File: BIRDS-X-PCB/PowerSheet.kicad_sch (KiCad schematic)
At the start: 28 parts, among them J201 Conn_01x02, J202 Conn_01x02, J203 Conn_01x02, Q201 AO3420, Q202 AO3420, U201 LTC4361-2, U202 LTC4361-2, U203 0.1S7B_0512S3UP

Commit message: Fix all DRC
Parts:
- removed JP201, JP202: Jumper_2_Open, Jumper:SolderJumper-2_P1.3mm_Open_RoundedPad1.0x1.5mm, symbol Jumper:Jumper_2_Open
- added Q502 (x2): 2N7002, Package_TO_SOT_SMD:SOT-23, symbol Transistor_FET:2N7002
- added R206, R207: 1M, Resistor_SMD:R_0603_1608Metric_Pad0.98x0.95mm_HandSolder, symbol Device:R
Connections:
- net DIO1_3V3_EN_FROM_BOSS: now also Q502.1 (G); no longer U202.1 (~{ON})
- net DIO2_5V_EN_FROM_BOSS: now also Q502.1 (G); no longer U201.1 (~{ON})
- net GND: now also Q502.2 (S), Q502.2 (S)
- net SUP_3V3: now also R207.1
- net SUP_5V0: now also R206.1
- new net: Q502.3 (D), R206.2, U201.1 (~{ON})
- new net: Q502.3 (D), R207.2, U202.1 (~{ON})
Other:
- note added: "Basic Inverter"

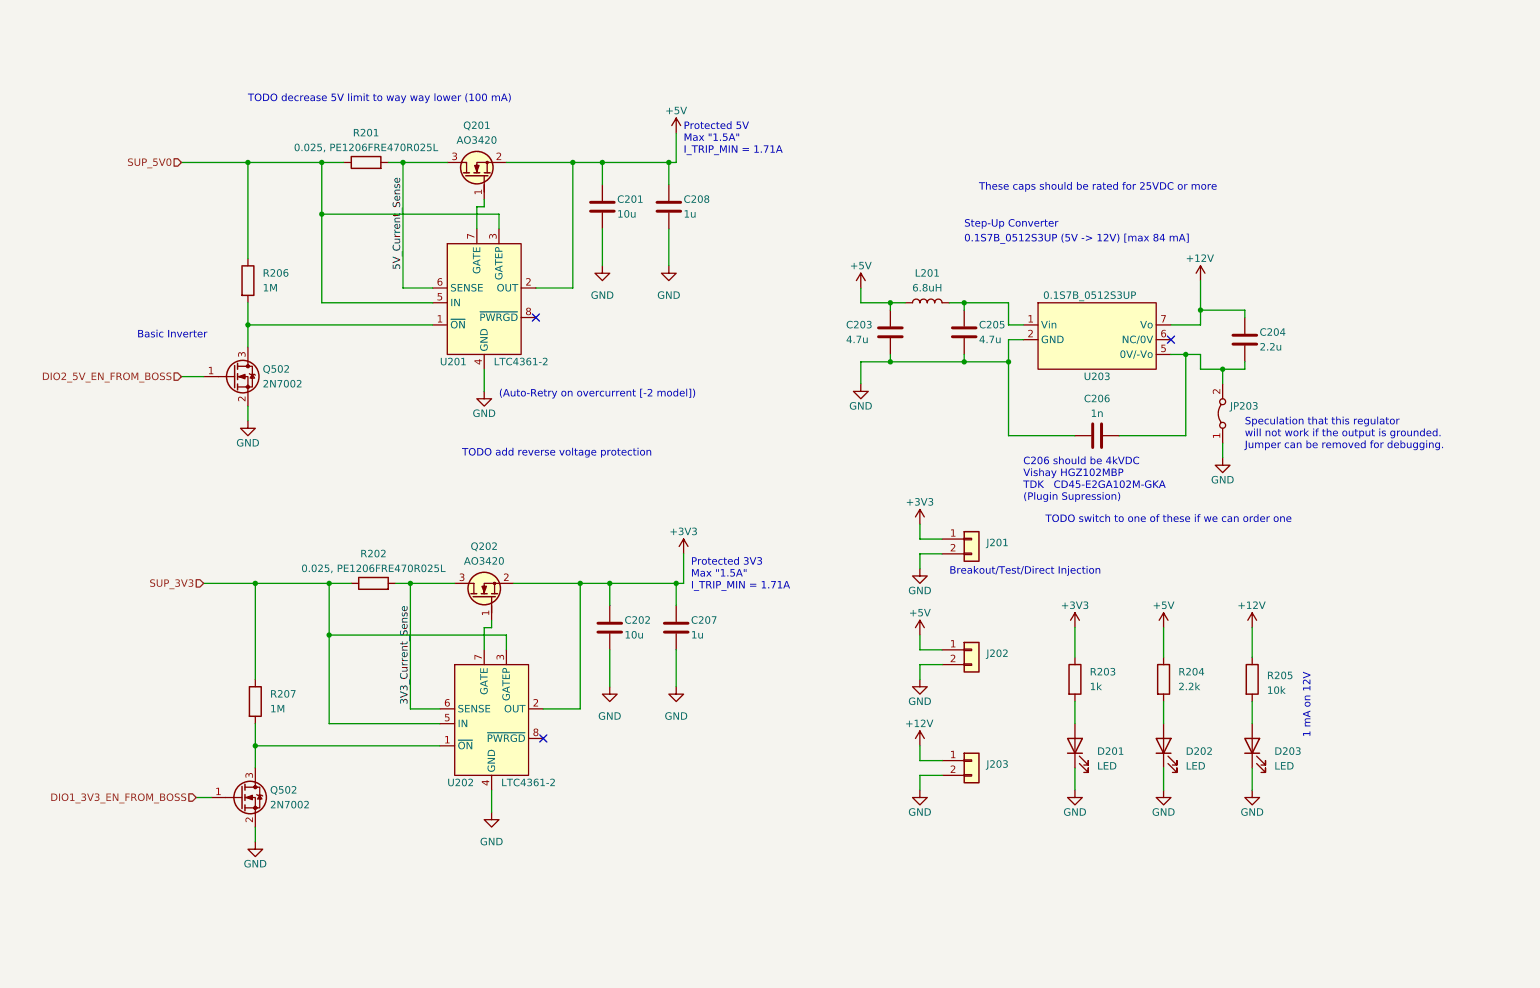
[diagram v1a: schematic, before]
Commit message: Update inverter resistors, add TPs
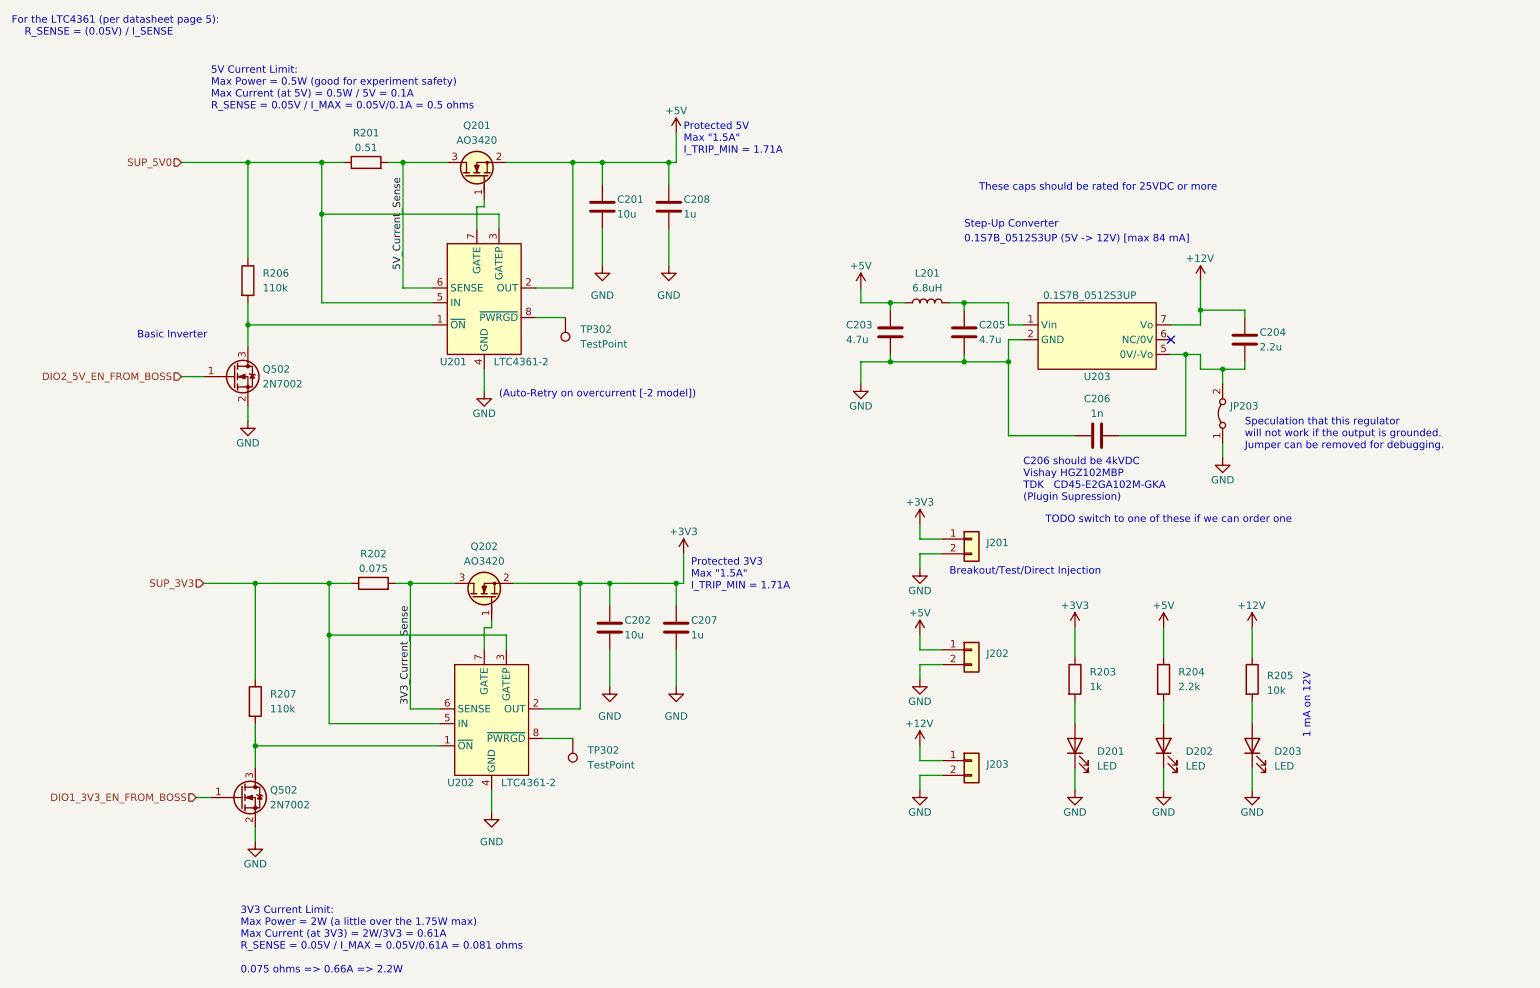
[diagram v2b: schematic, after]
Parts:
- added TP302 (x2): TestPoint, TestPoint:TestPoint_Pad_D1.5mm, symbol Connector:TestPoint
- R201: value 0.025, PE1206FRE470R025L -> 0.51; LCSC (none) -> C104948
- R202: value 0.025, PE1206FRE470R025L -> 0.075; LCSC (none) -> C171394
- R206, R207: value 1M -> 110k
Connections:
- net at U201.8 (~{PWRGD}): now also TP302.1
- net at U202.8 (~{PWRGD}): now also TP302.1
- no-connect marks 3 -> 1
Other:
- note added: "3V3 Current Limit: Max Power = 2W (a little over the 1.75W max) Max Current (at 3V3) = 2W/3V3 = 0.61A R_SENSE = 0.05V / I_MAX = 0.05V/0.61A = 0.081 ohms 0.075 ohms => 0.66A => 2.2W"
- note added: "5V Current Limit: Max Power = 0.5W (good for experiment safety) Max Current (at 5V) = 0.5W / 5V = 0.1A R_SENSE = 0.05V / I_MAX = 0.05V/0.1A = 0.5 ohms"
- note added: "For the LTC4361 (per datasheet page 5): R_SENSE = (0.05V) / I_SENSE"
- note removed: "TODO add reverse voltage protection"
- note removed: "TODO decrease 5V limit to way way lower (100 mA)"
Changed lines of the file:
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@@
   (junction (at 129.54 114.3) (diameter 0) (color 0 0 0 0)
   )
-  (no_connect (at 105.41 68.58))
   (no_connect (at 214.63 72.39))
-  (no_connect (at 106.68 140.97))
   (wire (pts (xy 198.12 88.9) (xy 186.69 88.9))
     (stroke (width 0) (type default))
@@
     (stroke (width 0) (type default))
   )
+  (wire (pts (xy 105.41 68.58) (xy 110.49 68.58))
+    (stroke (width 0) (type default))
+  )
   (wire (pts (xy 166.37 76.2) (xy 179.07 76.2))
     (stroke (width 0) (type default))
@@
   )
   (wire (pts (xy 128.27 41.91) (xy 128.27 45.72))
+    (stroke (width 0) (type default))
+  )
+  (wire (pts (xy 106.68 140.97) (xy 111.76 140.97))
     (stroke (width 0) (type default))
   )
@@
     (effects (font (size 1.27 1.27)) (justify left bottom))
   )
+  (text "For the LTC4361 (per datasheet page 5):\n    R_SENSE = (0.05V) / I_SENSE"
+    (at 15.24 20.32 0)
+    (effects (font (size 1.27 1.27)) (justify left bottom))
+  )
   (text "TODO switch to one of these if we can order one" (at 193.04 104.14 0)
     (effects (font (size 1.27 1.27)) (justify left bottom))
   )
   (text "Breakout/Test/Direct Injection" (at 176.53 113.03 0)
+    (effects (font (size 1.27 1.27)) (justify left bottom))
+  )
+  (text "3V3 Current Limit:\nMax Power = 2W (a little over the 1.75W max)\nMax Current (at 3V3) = 2W/3V3 = 0.61A\nR_SENSE = 0.05V / I_MAX = 0.05V/0.61A = 0.081 ohms\n\n0.075 ohms => 0.66A => 2.2W"
+    (at 54.61 181.61 0)
     (effects (font (size 1.27 1.27)) (justify left bottom))
   )
@@
     (effects (font (size 1.27 1.27)) (justify left bottom))
   )
+  (text "5V Current Limit:\nMax Power = 0.5W (good for experiment safety)\nMax Current (at 5V) = 0.5W / 5V = 0.1A\nR_SENSE = 0.05V / I_MAX = 0.05V/0.1A = 0.5 ohms"
+    (at 49.53 33.02 0)
+    (effects (font (size 1.27 1.27)) (justify left bottom))
+  )
   (text "(Auto-Retry on overcurrent [-2 model])" (at 99.06 82.55 0)
     (effects (font (size 1.27 1.27)) (justify left bottom))
@@
     (effects (font (size 1.27 1.27)) (justify left bottom))
   )
-  (text "TODO decrease 5V limit to way way lower (100 mA)" (at 55.88 31.75 0)
-    (effects (font (size 1.27 1.27)) (justify left bottom))
-  )
-  (text "TODO add reverse voltage protection" (at 92.71 92.71 0)
-    (effects (font (size 1.27 1.27)) (justify left bottom))
-  )
   (label "5V_Current_Sense" (at 82.55 44.45 270) (fields_autoplaced)
     (effects (font (size 1.27 1.27)) (justify right bottom))
@@
   (hierarchical_label "SUP_5V0" (shape input) (at 44.45 41.91 180) (fields_autoplaced)
     (effects (font (size 1.27 1.27)) (justify right))
+  )
+  (symbol (lib_id "Connector:TestPoint") (at 110.49 68.58 180) (unit 1)
+    (in_bom yes) (on_board yes) (dnp no) (fields_autoplaced)
+    (property "Reference" "TP302" (at 113.03 70.612 0)
+      (effects (font (size 1.27 1.27)) (justify right))
+    )
+    (property "Value" "TestPoint" (at 113.03 73.152 0)
+      (effects (font (size 1.27 1.27)) (justify right))
+    )
+    (property "Footprint" "TestPoint:TestPoint_Pad_D1.5mm" (at 105.41 68.58 0)
+      (effects (font (size 1.27 1.27)) hide)
+    )
+    (property "Datasheet" "~" (at 105.41 68.58 0)
+      (effects (font (size 1.27 1.27)) hide)
+    )
+    (pin "1")
+    (instances
+      (project "BIRDS-X-PCB"
+        (path "/c2796b15-795a-4d6e-ad4b-0ba87ded4bc9/adc73a10-1d27-484e-8ce9-d638694b8e29"
+          (reference "TP302") (unit 1)
+        )
+        (path "/c2796b15-795a-4d6e-ad4b-0ba87ded4bc9/f0b1214b-f453-423f-b2cf-f5d10e08eafe"
+          (reference "TP201") (unit 1)
+        )
+      )
+    )
   )
   (symbol (lib_id "power:GND") (at 128.27 59.69 0) (unit 1)
@@
       (effects (font (size 1.27 1.27)) (justify left))
     )
-    (property "Value" "1M" (at 59.69 135.89 0)
+    (property "Value" "110k" (at 59.69 135.89 0)
       (effects (font (size 1.27 1.27)) (justify left))
     )
@@
       (effects (font (size 1.27 1.27)))
     )
-    (property "Value" "0.025, PE1206FRE470R025L" (at 76.2 39.37 90)
+    (property "Value" "0.51" (at 76.2 39.37 90)
       (effects (font (size 1.27 1.27)))
     )
@@
       (effects (font (size 1.27 1.27)) hide)
     )
+    (property "LCSC" "C104948" (at 76.2 41.91 90)
+      (effects (font (size 1.27 1.27)) hide)
+    )
     (pin "1")
     (pin "2")
@@
       (effects (font (size 1.27 1.27)) (justify left))
     )
-    (property "Value" "1M" (at 58.42 63.5 0)
+    (property "Value" "110k" (at 58.42 63.5 0)
       (effects (font (size 1.27 1.27)) (justify left))
     )
@@
       (effects (font (size 1.27 1.27)))
     )
-    (property "Value" "0.025, PE1206FRE470R025L" (at 77.47 111.76 90)
+    (property "Value" "0.075" (at 77.47 111.76 90)
       (effects (font (size 1.27 1.27)))
     )
@@
     )
     (property "Datasheet" "~" (at 77.47 114.3 0)
+      (effects (font (size 1.27 1.27)) hide)
+    )
+    (property "LCSC" "C171394" (at 77.47 114.3 90)
       (effects (font (size 1.27 1.27)) hide)
     )
@@
         )
       )
+    )
+  )
+  (symbol (lib_id "Connector:TestPoint") (at 111.76 140.97 180) (unit 1)
+    (in_bom yes) (on_board yes) (dnp no) (fields_autoplaced)
+    (property "Reference" "TP302" (at 114.3 143.002 0)
+      (effects (font (size 1.27 1.27)) (justify right))
+    )
+    (property "Value" "TestPoint" (at 114.3 145.542 0)
+      (effects (font (size 1.27 1.27)) (justify right))
+    )
+    (property "Footprint" "TestPoint:TestPoint_Pad_D1.5mm" (at 106.68 140.97 0)
+      (effects (font (size 1.27 1.27)) hide)
+    )
+    (property "Datasheet" "~" (at 106.68 140.97 0)
+      (effects (font (size 1.27 1.27)) hide)
+    )
+    (pin "1")
+    (instances
+      (project "BIRDS-X-PCB"
+        (path "/c2796b15-795a-4d6e-ad4b-0ba87ded4bc9/adc73a10-1d27-484e-8ce9-d638694b8e29"
+          (reference "TP302") (unit 1)
+        )
+        (path "/c2796b15-795a-4d6e-ad4b-0ba87ded4bc9/f0b1214b-f453-423f-b2cf-f5d10e08eafe"
+          (reference "TP202") (unit 1)
+        )
+      )

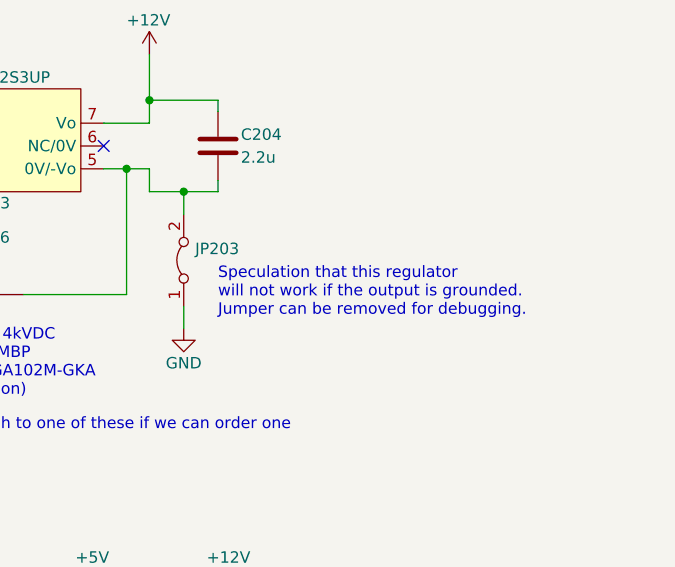
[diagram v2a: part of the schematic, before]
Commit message: Refactor jumper for PIN experiment power
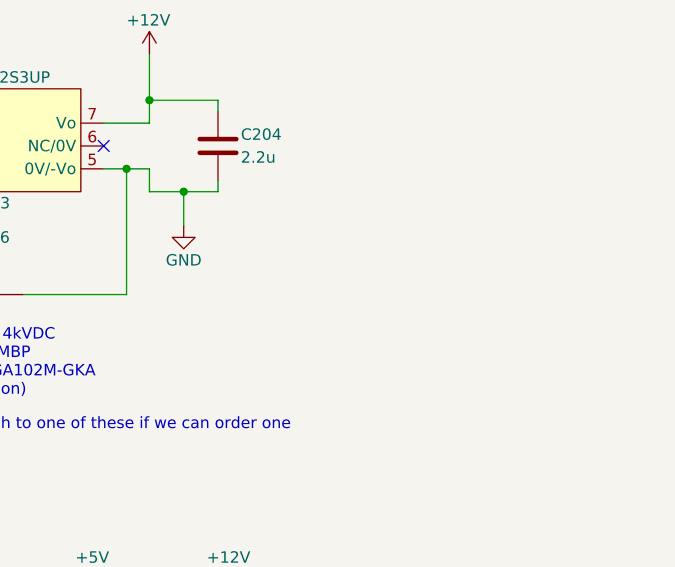
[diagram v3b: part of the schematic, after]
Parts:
- removed JP203: Jumper_2_Bridged, Jumper:SolderJumper-2_P1.3mm_Open_RoundedPad1.0x1.5mm, symbol Jumper:Jumper_2_Bridged
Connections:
- net GND: now also C204.2, C206.1, U203.5 (0V/-Vo)
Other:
- note removed: "Speculation that this regulator will not work if the output is grounded. Jumper can be removed for debugging."
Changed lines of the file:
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@@
-    (stroke (width 0) (type default))
-  )
-  (wire (pts (xy 223.52 77.47) (xy 223.52 80.01))
     (stroke (width 0) (type default))
   )
@@
     (stroke (width 0) (type default))
   )
-  (wire (pts (xy 223.52 90.17) (xy 223.52 92.71))
+  (wire (pts (xy 223.52 77.47) (xy 223.52 81.28))
     (stroke (width 0) (type default))
   )
@@
     (effects (font (size 1.27 1.27)) (justify left bottom))
   )
-  (text "Speculation that this regulator\nwill not work if the output is grounded.\nJumper can be removed for debugging."
-    (at 227.33 91.44 0)
-    (effects (font (size 1.27 1.27)) (justify left bottom))
-  )
   (text "0.1S7B_0512S3UP (5V -> 12V) [max 84 mA]" (at 179.07 55.88 0)
     (effects (font (size 1.27 1.27)) (justify left bottom))
@@
         (path "/c2796b15-795a-4d6e-ad4b-0ba87ded4bc9/f0b1214b-f453-423f-b2cf-f5d10e08eafe"
           (reference "#PWR015") (unit 1)
-        )
-      )
-    )
-  )
-  (symbol (lib_id "Jumper:Jumper_2_Bridged") (at 223.52 85.09 90) (unit 1)
-    (in_bom yes) (on_board yes) (dnp no) (fields_autoplaced)
-    (property "Reference" "JP203" (at 224.79 83.82 90)
-      (effects (font (size 1.27 1.27)) (justify right))
-    )
-    (property "Value" "Jumper_2_Bridged" (at 224.79 86.36 90)
-      (effects (font (size 1.27 1.27)) (justify right) hide)
-    )
-    (property "Footprint" "Jumper:SolderJumper-2_P1.3mm_Open_RoundedPad1.0x1.5mm" (at 223.52 85.09 0)
-      (effects (font (size 1.27 1.27)) hide)
-    )
-    (property "Datasheet" "~" (at 223.52 85.09 0)
-      (effects (font (size 1.27 1.27)) hide)
-    )
-    (pin "1")
-    (pin "2")
-    (instances
-      (project "BIRDS-X-PCB"
-        (path "/c2796b15-795a-4d6e-ad4b-0ba87ded4bc9/f0b1214b-f453-423f-b2cf-f5d10e08eafe"
-          (reference "JP203") (unit 1)
         )
       )
@@
     )
   )
-  (symbol (lib_id "power:GND") (at 223.52 92.71 0) (unit 1)
-    (in_bom yes) (on_board yes) (dnp no)
-    (property "Reference" "#PWR08" (at 223.52 99.06 0)
-      (effects (font (size 1.27 1.27)) hide)
-    )
-    (property "Value" "GND" (at 223.52 96.52 0)
-      (effects (font (size 1.27 1.27)))
-    )
-    (property "Footprint" "" (at 223.52 92.71 0)
-      (effects (font (size 1.27 1.27)) hide)
-    )
-    (property "Datasheet" "" (at 223.52 92.71 0)
-      (effects (font (size 1.27 1.27)) hide)
-    )
+  (symbol (lib_id "power:GND") (at 223.52 81.28 0) (unit 1)
+    (in_bom yes) (on_board yes) (dnp no)
+    (property "Reference" "#PWR08" (at 223.52 87.63 0)
+      (effects (font (size 1.27 1.27)) hide)
+    )
+    (property "Value" "GND" (at 223.52 85.09 0)
+      (effects (font (size 1.27 1.27)))
+    )
+    (property "Footprint" "" (at 223.52 81.28 0)
+      (effects (font (size 1.27 1.27)) hide)
+    )
+    (property "Datasheet" "" (at 223.52 81.28 0)
+      (effects (font (size 1.27 1.27)) hide)
+    )
